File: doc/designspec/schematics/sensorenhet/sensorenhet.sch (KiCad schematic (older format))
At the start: 7 parts, among them IC1 ATMEGA1284P-P, U1 IQEXO-3, U2 Terminator-CTRL, U3 USB-UART, U4 Lidar_Lite_v2

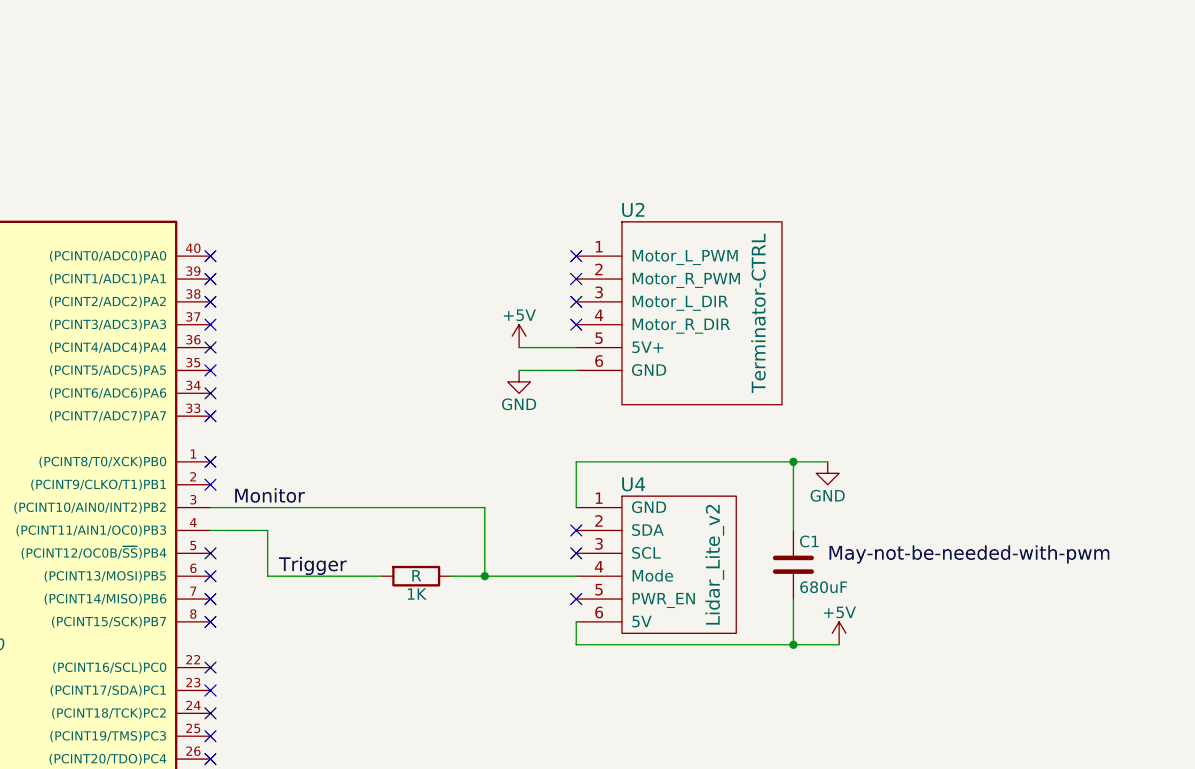
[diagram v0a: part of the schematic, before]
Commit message: Add IR sensors
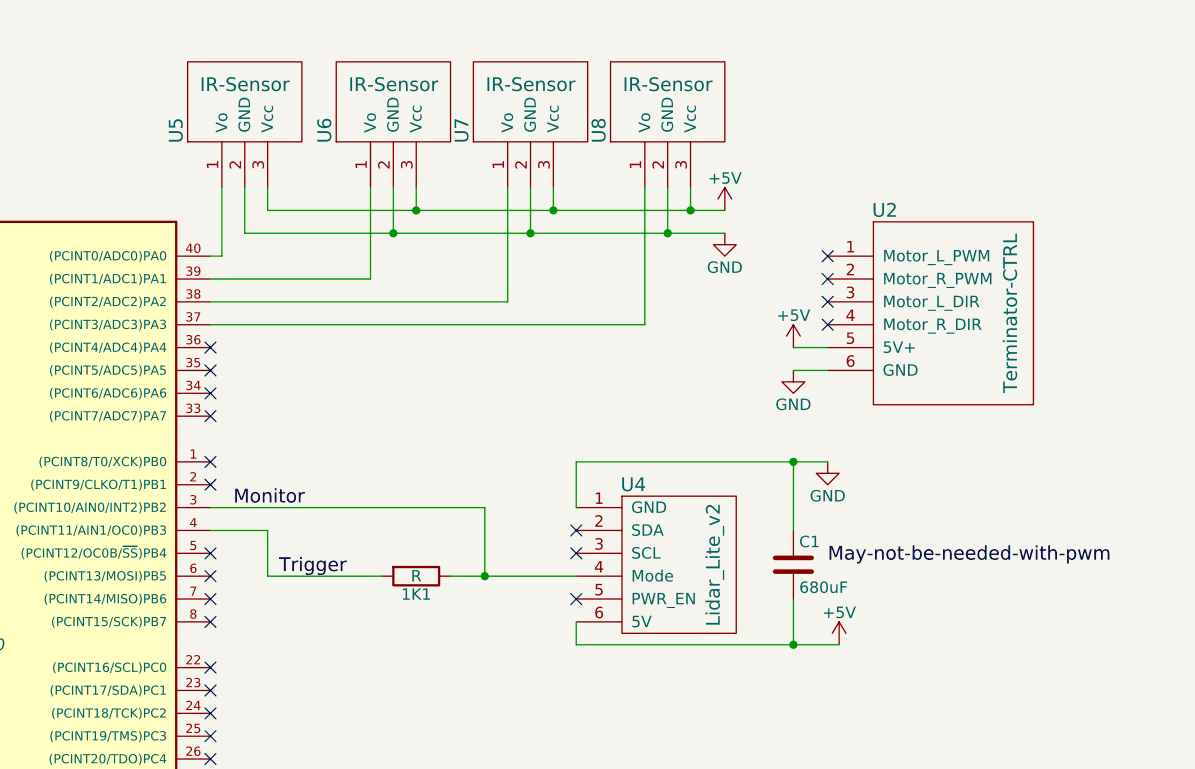
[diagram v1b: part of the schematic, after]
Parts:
- added U5, U6, U7, U8: IR-Sensor, symbol IR-Sensor
- renumbered 1K to 1K1
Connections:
- net +5V: now also U5.3 (Vcc), U6.3 (Vcc), U7.3 (Vcc), U8.3 (Vcc)
- net GND: now also U5.2 (GND), U6.2 (GND), U7.2 (GND), U8.2 (GND)
- net at IC1.37 ((PCINT3/ADC3)PA3): now also U8.1 (Vo)
- net at IC1.38 ((PCINT2/ADC2)PA2): now also U7.1 (Vo)
- net at IC1.39 ((PCINT1/ADC1)PA1): now also U6.1 (Vo)
- net at IC1.40 ((PCINT0/ADC0)PA0): now also U5.1 (Vo)
- no-connect marks 38 -> 34
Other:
- moved on the sheet: U2
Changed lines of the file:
@@
 Text GLabel 3750 2000 0    60   Input ~ 0
 RESET
-NoConn ~ 5750 2100
-NoConn ~ 5750 2200
 NoConn ~ 1750 2000
-NoConn ~ 5750 2300
 NoConn ~ 5750 2400
 NoConn ~ 5750 2500
@@
 L Terminator-CTRL U2
 U 1 1 57FA7BA2
-P 8150 2200
-F 0 "U2" H 7600 2600 60  0000 C CNN
-F 1 "Terminator-CTRL" V 8150 2150 60  0000 C CNN
-F 2 "" H 8150 2200 60  0001 C CNN
-F 3 "" H 8150 2200 60  0001 C CNN
-	1    8150 2200
-	1    0    0    -1
-$EndComp
-NoConn ~ 7350 2000
-NoConn ~ 7350 2100
-NoConn ~ 7350 2200
-NoConn ~ 7350 2300
+P 9250 2200
+F 0 "U2" H 8700 2600 60  0000 C CNN
+F 1 "Terminator-CTRL" V 9250 2150 60  0000 C CNN
+F 2 "" H 9250 2200 60  0001 C CNN
+F 3 "" H 9250 2200 60  0001 C CNN
+	1    9250 2200
+	1    0    0    -1
+$EndComp
+NoConn ~ 8450 2000
+NoConn ~ 8450 2100
+NoConn ~ 8450 2200
+NoConn ~ 8450 2300
 $Comp
 L +5V #PWR07
 U 1 1 57FA7CB1
-P 7100 2400
-F 0 "#PWR07" H 7100 2250 50  0001 C CNN
-F 1 "+5V" H 7100 2540 50  0000 C CNN
-F 2 "" H 7100 2400 50  0000 C CNN
-F 3 "" H 7100 2400 50  0000 C CNN
-	1    7100 2400
+P 8300 2400
+F 0 "#PWR07" H 8300 2250 50  0001 C CNN
+F 1 "+5V" H 8300 2540 50  0000 C CNN
+F 2 "" H 8300 2400 50  0000 C CNN
+F 3 "" H 8300 2400 50  0000 C CNN
+	1    8300 2400
 	1    0    0    -1
 $EndComp
@@
 L GND #PWR08
 U 1 1 57FA7CCD
-P 7100 2500
-F 0 "#PWR08" H 7100 2250 50  0001 C CNN
-F 1 "GND" H 7100 2350 50  0000 C CNN
-F 2 "" H 7100 2500 50  0000 C CNN
-F 3 "" H 7100 2500 50  0000 C CNN
-	1    7100 2500
+P 8300 2500
+F 0 "#PWR08" H 8300 2250 50  0001 C CNN
+F 1 "GND" H 8300 2350 50  0000 C CNN
+F 2 "" H 8300 2500 50  0000 C CNN
+F 3 "" H 8300 2500 50  0000 C CNN
+	1    8300 2500
 	1    0    0    -1
 $EndComp
@@
 Text Label 8450 3350 0    60   ~ 0
 May-not-be-needed-with-pwm
-NoConn ~ 5750 2000
-Wire Wire Line
-	4750 1150 4750 1700
-Wire Wire Line
-	4550 5700 4750 5700
-Wire Wire Line
-	4750 5700 4750 5850
-Connection ~ 4750 5700
-Wire Wire Line
-	1750 2100 1450 2100
-Wire Wire Line
-	1450 2100 1450 2800
-Wire Wire Line
-	2800 2300 2650 2300
-Wire Wire Line
-	2800 2100 2800 2450
-Wire Wire Line
-	2650 2200 3000 2200
-Connection ~ 2800 2200
-Wire Wire Line
-	2650 2100 2800 2100
-Wire Wire Line
-	2650 2000 3000 2000
-Wire Wire Line
-	1750 2000 1500 2000
-Wire Wire Line
-	1450 2800 3750 2800
-Wire Wire Line
-	1750 2300 1750 2450
-Wire Wire Line
-	1750 2450 2800 2450
-Connection ~ 2800 2300
-Wire Wire Line
-	4300 1600 4550 1600
-Wire Wire Line
-	4550 1600 4550 1700
-Wire Wire Line
-	1750 2200 1650 2200
-Wire Wire Line
-	1650 2200 1650 2350
-Wire Wire Line
-	1650 2350 1550 2350
-Wire Wire Line
-	1550 2350 1550 2300
-Wire Wire Line
-	7350 2500 7100 2500
-Wire Wire Line
-	7350 2400 7100 2400
-Wire Wire Line
-	7350 3700 8500 3700
-Wire Wire Line
-	7350 3700 7350 3600
-Wire Wire Line
-	7350 2900 8450 2900
-Wire Wire Line
-	7350 2900 7350 3100
-Wire Wire Line
-	8300 3500 8300 3700
-Connection ~ 8300 3700
-Wire Wire Line
-	8300 3200 8300 2900
-Connection ~ 8300 2900
-Wire Wire Line
-	5750 3200 6000 3200
-Wire Wire Line
-	6000 3200 6000 3400
 Text Label 5850 3100 0    60   ~ 0
 Monitor
@@
 NoConn ~ 7350 3300
 NoConn ~ 7350 3500
-Wire Wire Line
-	5750 3100 6950 3100
-$Comp
-L R 1K
+$Comp
+L R 1K1
 U 1 1 57FA84DB
 P 6650 3400
-F 0 "1K" V 6730 3400 50  0000 C CNN
+F 0 "1K1" V 6730 3400 50  0000 C CNN
 F 1 "R" V 6650 3400 50  0000 C CNN
 F 2 "" V 6580 3400 50  0000 C CNN
@@
 	0    1    1    0
 $EndComp
+$Comp
+L IR-Sensor U6
+U 1 1 57FA8A40
+P 6550 1250
+F 0 "U6" H 6350 1550 60  0000 C CNN
+F 1 "IR-Sensor" V 6550 1250 60  0000 C CNN
+F 2 "" H 6550 1250 60  0001 C CNN
+F 3 "" H 6550 1250 60  0001 C CNN
+	1    6550 1250
+	0    -1   -1   0
+$EndComp
+$Comp
+L IR-Sensor U7
+U 1 1 57FA8D52
+P 7150 1250
+F 0 "U7" H 6950 1550 60  0000 C CNN
+F 1 "IR-Sensor" V 7150 1250 60  0000 C CNN
+F 2 "" H 7150 1250 60  0001 C CNN
+F 3 "" H 7150 1250 60  0001 C CNN
+	1    7150 1250
+	0    -1   -1   0
+$EndComp
+$Comp
+L IR-Sensor U8
+U 1 1 57FA8E11
+P 7750 1250
+F 0 "U8" H 7550 1550 60  0000 C CNN
+F 1 "IR-Sensor" V 7750 1250 60  0000 C CNN
+F 2 "" H 7750 1250 60  0001 C CNN
+F 3 "" H 7750 1250 60  0001 C CNN
+	1    7750 1250
+	0    -1   -1   0
+$EndComp
+$Comp
+L IR-Sensor U5
+U 1 1 57FA8E73
+P 5900 1250
+F 0 "U5" H 5700 1550 60  0000 C CNN
+F 1 "IR-Sensor" V 5900 1250 60  0000 C CNN
+F 2 "" H 5900 1250 60  0001 C CNN
+F 3 "" H 5900 1250 60  0001 C CNN
+	1    5900 1250
+	0    -1   -1   0
+$EndComp
+Wire Wire Line
+	4750 1150 4750 1700
+Wire Wire Line
+	4550 5700 4750 5700
+Wire Wire Line
+	4750 5700 4750 5850
+Connection ~ 4750 5700
+Wire Wire Line
+	1750 2100 1450 2100
+Wire Wire Line
+	1450 2100 1450 2800
+Wire Wire Line
+	2800 2300 2650 2300
+Wire Wire Line
+	2800 2100 2800 2450
+Wire Wire Line
+	2650 2200 3000 2200
+Connection ~ 2800 2200
+Wire Wire Line
+	2650 2100 2800 2100
+Wire Wire Line
+	2650 2000 3000 2000
+Wire Wire Line
+	1750 2000 1500 2000
+Wire Wire Line
+	1450 2800 3750 2800
+Wire Wire Line
+	1750 2300 1750 2450
+Wire Wire Line
+	1750 2450 2800 2450
+Connection ~ 2800 2300
+Wire Wire Line
+	4300 1600 4550 1600
+Wire Wire Line
+	4550 1600 4550 1700
+Wire Wire Line
+	1750 2200 1650 2200
+Wire Wire Line
+	1650 2200 1650 2350
+Wire Wire Line
+	1650 2350 1550 2350
+Wire Wire Line
+	1550 2350 1550 2300
+Wire Wire Line
+	8450 2500 8300 2500
+Wire Wire Line
+	8450 2400 8300 2400
+Wire Wire Line
+	7350 3700 8500 3700
+Wire Wire Line
+	7350 3700 7350 3600
+Wire Wire Line
+	7350 2900 8450 2900
+Wire Wire Line
+	7350 2900 7350 3100
+Wire Wire Line
+	8300 3500 8300 3700
+Connection ~ 8300 3700
+Wire Wire Line
+	8300 3200 8300 2900
+Connection ~ 8300 2900
+Wire Wire Line
+	5750 3200 6000 3200
+Wire Wire Line
+	6000 3200 6000 3400
+Wire Wire Line
+	5750 3100 6950 3100
 Wire Wire Line
 	6950 3100 6950 3400
@@
 	6800 3400 7350 3400
 Connection ~ 6950 3400
+Wire Wire Line
+	5800 1700 5800 2000
+Wire Wire Line
+	5800 2000 5750 2000
+Wire Wire Line
+	6450 1700 6450 2100
+Wire Wire Line
+	6450 2100 5750 2100
+Wire Wire Line
+	7050 1700 7050 2200
+Wire Wire Line
+	7050 2200 5750 2200
+Wire Wire Line
+	7650 1700 7650 2300
+Wire Wire Line
+	7650 2300 5750 2300
+Wire Wire Line
+	5900 1700 5900 1900
+Wire Wire Line
+	5900 1900 8000 1900
+Wire Wire Line
+	7750 1700 7750 1900
+Connection ~ 7750 1900
+Wire Wire Line
+	7150 1700 7150 1900
+Connection ~ 7150 1900
+Wire Wire Line
+	6550 1700 6550 1900
+Connection ~ 6550 1900
+Wire Wire Line
+	6000 1700 6000 1800
+Wire Wire Line
+	6000 1800 8000 1800
+Wire Wire Line
+	7850 1700 7850 1800
+Connection ~ 7850 1800
+Wire Wire Line
+	7250 1700 7250 1800
+Connection ~ 7250 1800
+Wire Wire Line
+	6650 1700 6650 1800
+Connection ~ 6650 1800
+$Comp
+L +5V #PWR011
+U 1 1 57FA9432
+P 8000 1800
+F 0 "#PWR011" H 8000 1650 50  0001 C CNN
+F 1 "+5V" H 8000 1940 50  0000 C CNN
+F 2 "" H 8000 1800 50  0000 C CNN
+F 3 "" H 8000 1800 50  0000 C CNN
+	1    8000 1800
+	1    0    0    -1
+$EndComp
+$Comp
+L GND #PWR012
+U 1 1 57FA945C
+P 8000 1900
+F 0 "#PWR012" H 8000 1650 50  0001 C CNN
+F 1 "GND" H 8000 1750 50  0000 C CNN
+F 2 "" H 8000 1900 50  0000 C CNN
+F 3 "" H 8000 1900 50  0000 C CNN
+	1    8000 1900
+	1    0    0    -1
+$EndComp
 $EndSCHEMATC

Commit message: Remove front IR sensor
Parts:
- removed U8: IR-Sensor, symbol IR-Sensor
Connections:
- no-connect marks 34 -> 35
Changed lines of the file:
@@
-$EndComp
-$Comp
-L IR-Sensor U8
-U 1 1 57FA8E11
-P 7750 1250
-F 0 "U8" H 7550 1550 60  0000 C CNN
-F 1 "IR-Sensor" V 7750 1250 60  0000 C CNN
-F 2 "" H 7750 1250 60  0001 C CNN
-F 3 "" H 7750 1250 60  0001 C CNN
-	1    7750 1250
-	0    -1   -1   0
 $EndComp
 $Comp
@@
 	2800 2300 2650 2300
 Wire Wire Line
-	2800 2100 2800 2450
+	2800 2100 2800 2200
 Wire Wire Line
-	2650 2200 3000 2200
+	2800 2200 2800 2300
+Wire Wire Line
+	2800 2300 2800 2450
+Wire Wire Line
+	2650 2200 2800 2200
+Wire Wire Line
+	2800 2200 3000 2200
 Connection ~ 2800 2200
 Wire Wire Line
@@
 	8450 2400 8300 2400
 Wire Wire Line
-	7350 3700 8500 3700
+	7350 3700 8300 3700
+Wire Wire Line
+	8300 3700 8500 3700
 Wire Wire Line
 	7350 3700 7350 3600
 Wire Wire Line
-	7350 2900 8450 2900
+	7350 2900 8300 2900
+Wire Wire Line
+	8300 2900 8450 2900
 Wire Wire Line
 	7350 2900 7350 3100
@@
 	6000 3400 6500 3400
 Wire Wire Line
-	6800 3400 7350 3400
+	6800 3400 6950 3400
+Wire Wire Line
+	6950 3400 7350 3400
 Connection ~ 6950 3400
 Wire Wire Line
@@
 	7050 2200 5750 2200
 Wire Wire Line
-	7650 1700 7650 2300
-Wire Wire Line
-	7650 2300 5750 2300
-Wire Wire Line
 	5900 1700 5900 1900
 Wire Wire Line
-	5900 1900 8000 1900
+	5900 1900 6550 1900
 Wire Wire Line
-	7750 1700 7750 1900
-Connection ~ 7750 1900
+	6550 1900 7150 1900
+Wire Wire Line
+	7150 1900 7600 1900
 Wire Wire Line
 	7150 1700 7150 1900
@@
 	6000 1700 6000 1800
 Wire Wire Line
-	6000 1800 8000 1800
+	6000 1800 6650 1800
 Wire Wire Line
-	7850 1700 7850 1800
-Connection ~ 7850 1800
+	6650 1800 7250 1800
+Wire Wire Line
+	7250 1800 7600 1800
 Wire Wire Line
 	7250 1700 7250 1800
@@
 L +5V #PWR011
 U 1 1 57FA9432
-P 8000 1800
-F 0 "#PWR011" H 8000 1650 50  0001 C CNN
-F 1 "+5V" H 8000 1940 50  0000 C CNN
-F 2 "" H 8000 1800 50  0000 C CNN
-F 3 "" H 8000 1800 50  0000 C CNN
-	1    8000 1800
+P 7600 1800
+F 0 "#PWR011" H 7600 1650 50  0001 C CNN
+F 1 "+5V" H 7600 1940 50  0000 C CNN
+F 2 "" H 7600 1800 50  0000 C CNN
+F 3 "" H 7600 1800 50  0000 C CNN
+	1    7600 1800
 	1    0    0    -1
 $EndComp
@@
 L GND #PWR012
 U 1 1 57FA945C
-P 8000 1900
-F 0 "#PWR012" H 8000 1650 50  0001 C CNN
-F 1 "GND" H 8000 1750 50  0000 C CNN
-F 2 "" H 8000 1900 50  0000 C CNN
-F 3 "" H 8000 1900 50  0000 C CNN
-	1    8000 1900
+P 7600 1900
+F 0 "#PWR012" H 7600 1650 50  0001 C CNN
+F 1 "GND" H 7600 1750 50  0000 C CNN
+F 2 "" H 7600 1900 50  0000 C CNN
+F 3 "" H 7600 1900 50  0000 C CNN
+	1    7600 1900
 	1    0    0    -1
 $EndComp
+NoConn ~ 5750 2300
 $EndSCHEMATC
